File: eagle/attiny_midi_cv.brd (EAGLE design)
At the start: 100.9 x 80.9 mm, 26 parts, among them IC1 TL072P, Q518 2N3904, U2 TINY45-20-DIP

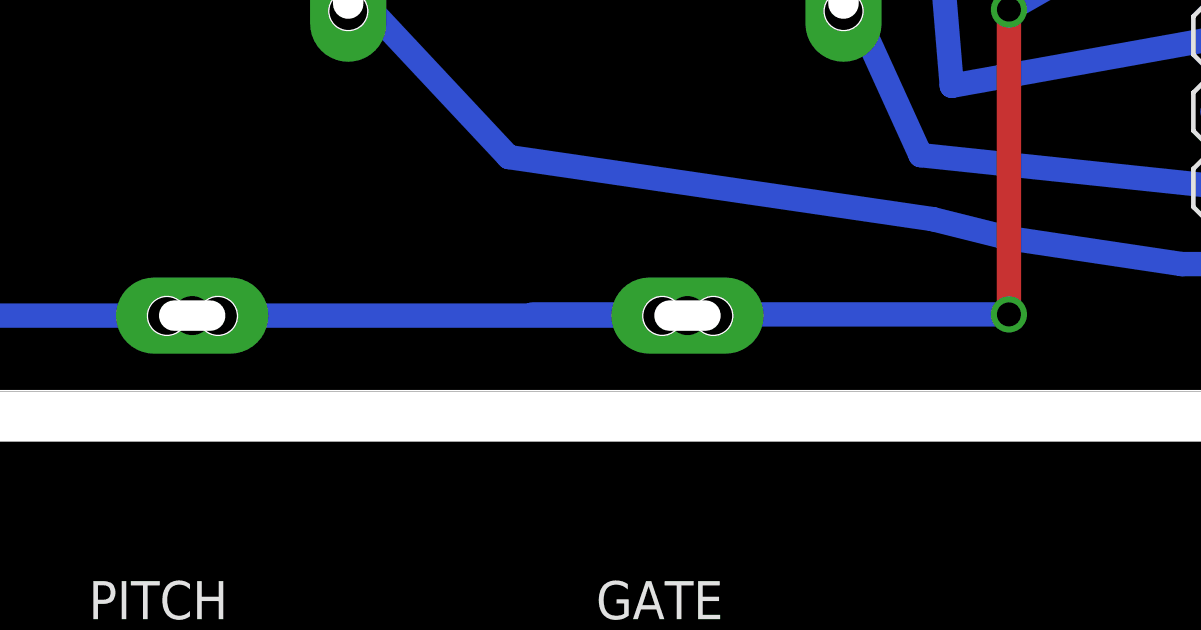
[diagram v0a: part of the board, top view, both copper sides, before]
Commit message: fixed overlap in gnd route
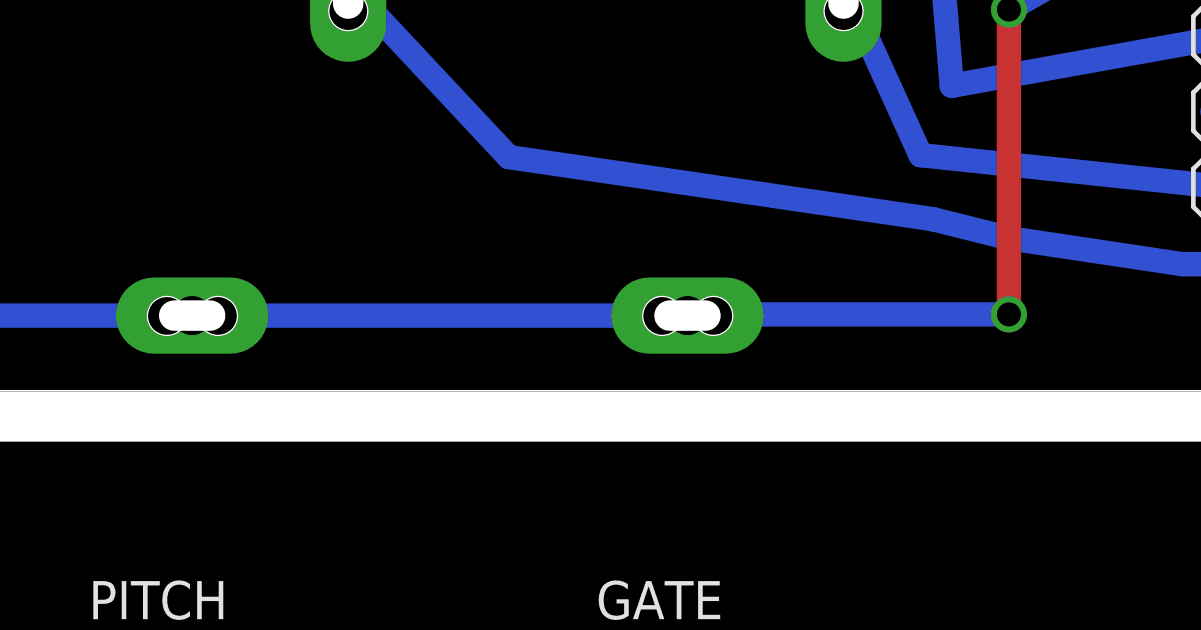
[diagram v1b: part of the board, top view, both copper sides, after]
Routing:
- net N$10: track 165.3 -> 160.2 mm
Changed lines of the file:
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@@
 </signal>
 <signal name="N$10">
-<wire x1="36.83" y1="2.54" x2="52.705" y2="2.54" width="0.8128" layer="16"/>
 <contactref element="OK1" pad="5"/>
 <contactref element="U$4" pad="5"/>
@@
 <wire x1="8.97" y1="2.5" x2="18.1102" y2="2.5" width="0.8128" layer="16"/>
 <wire x1="18.1102" y1="2.5" x2="25.48" y2="2.5" width="0.8128" layer="16"/>
-<wire x1="25.48" y1="2.5" x2="41.99" y2="2.5" width="0.8128" layer="16"/>
 <wire x1="22.225" y1="23.495" x2="18.1102" y2="22.225" width="0.8128" layer="16"/>
 <wire x1="18.1102" y1="22.225" x2="18.1102" y2="2.5" width="0.8128" layer="16"/>
 <wire x1="52.705" y1="12.7" x2="60.1218" y2="16.9164" width="0.8128" layer="16"/>
-<wire x1="41.99" y1="2.5" x2="36.83" y2="2.54" width="0" layer="19" extent="16-16"/>
 <via x="52.705" y="12.7" extent="1-16" drill="0.8" shape="square"/>
 <wire x1="52.705" y1="12.7" x2="52.705" y2="2.54" width="0.8128" layer="1"/>
 <via x="52.705" y="2.54" extent="1-16" drill="0.8" shape="square"/>
+<wire x1="52.705" y1="2.54" x2="42.03" y2="2.54" width="0.8128" layer="16"/>
+<wire x1="42.03" y1="2.54" x2="41.99" y2="2.5" width="0.8128" layer="16"/>
+<wire x1="41.99" y1="2.5" x2="25.48" y2="2.5" width="0.8128" layer="16"/>
 </signal>
 </signals>
